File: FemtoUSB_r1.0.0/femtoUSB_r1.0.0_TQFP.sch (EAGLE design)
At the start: 24 parts, among them IC1 ATSAMD21E18A-AU

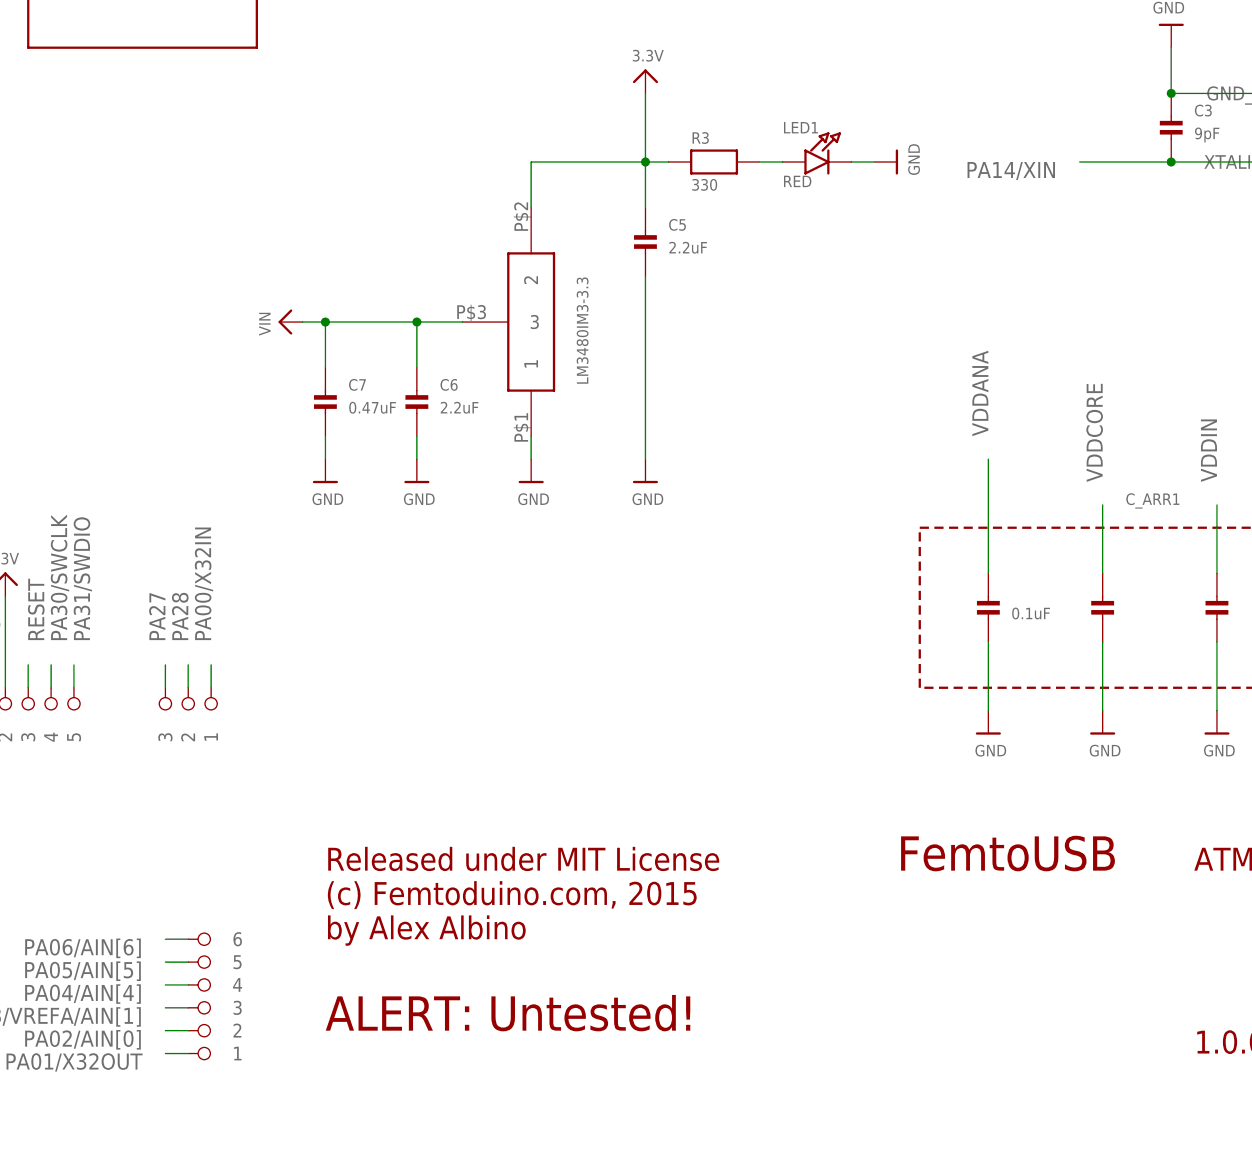
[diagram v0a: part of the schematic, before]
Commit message: Corrected the Make and model of the LDO Voltage Regulator. Board now powers on.
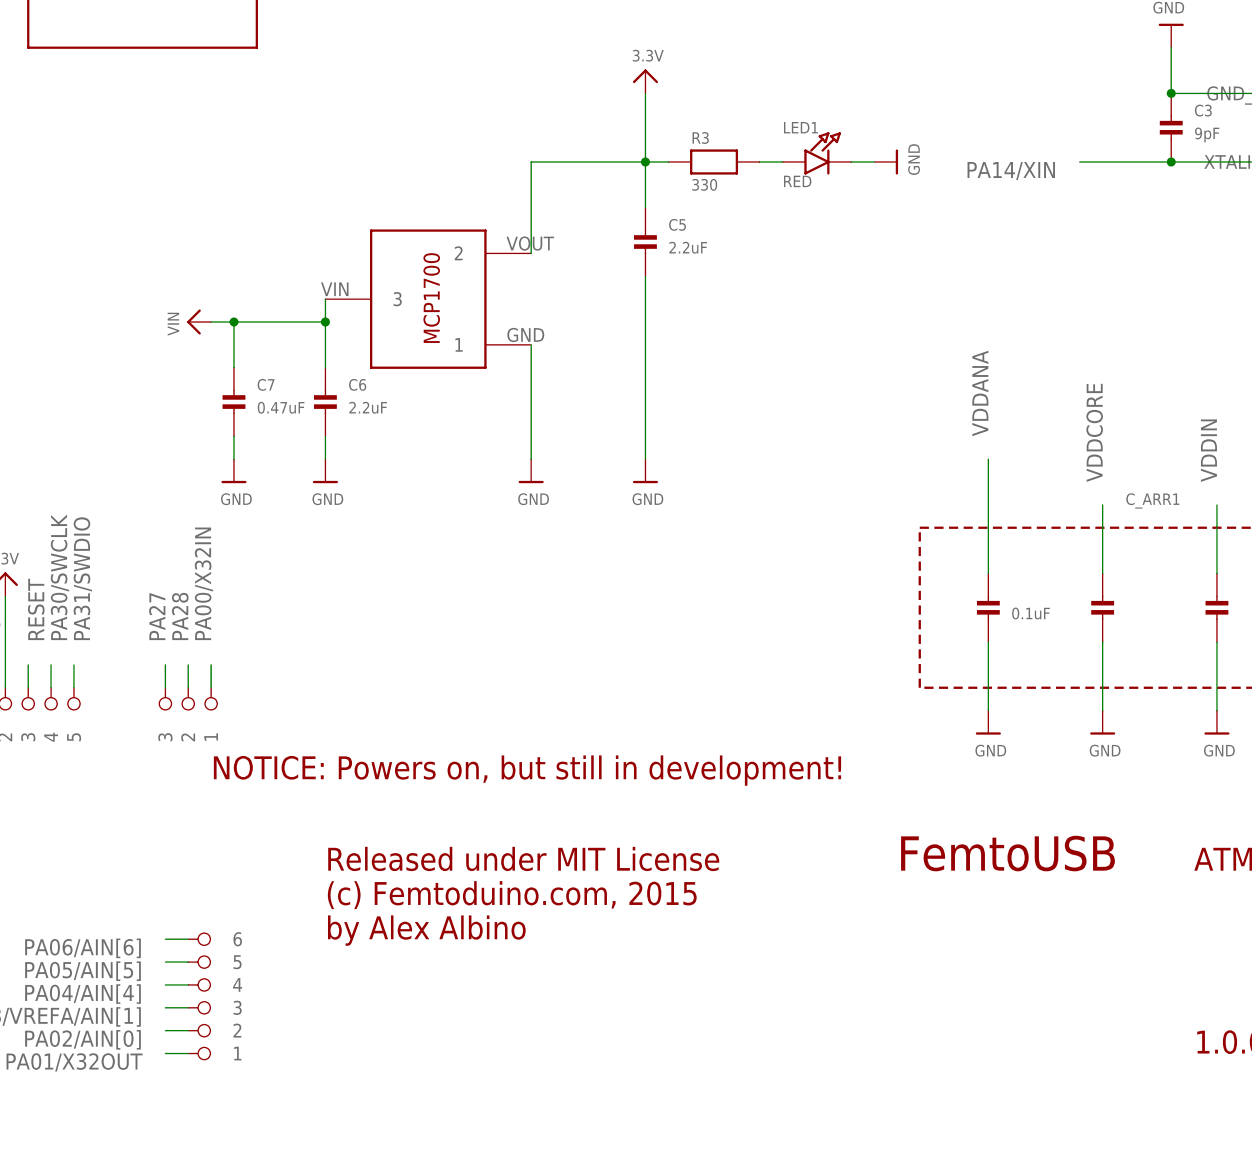
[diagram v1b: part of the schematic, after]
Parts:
- LDO_VREG: value LM3480 -> MCP1700T-3302E/TT; device ti-lm3480:LM3480 -> MCP1700T-3302E_TT:MCP1700T-3302E/TT
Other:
- note added: "NOTICE: Powers on, but still in development!"
- note removed: "ALERT: Untested!"
- moved on the sheet: C6, C7
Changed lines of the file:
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@@
 <part name="U$26" library="microbuilder" deviceset="GND" device=""/>
 <part name="U$27" library="microbuilder" deviceset="GND" device=""/>
-<part name="LDO_VREG" library="ti-lm3480" deviceset="LM3480" device=""/>
+<part name="LDO_VREG" library="MCP1700T-3302E_TT" deviceset="MCP1700T-3302E/TT" device=""/>
 <part name="U$3" library="microbuilder" deviceset="GND" device=""/>
 <part name="C5" library="microbuilder" deviceset="CAP_CERAMIC" device="_0402MP" value="2.2uF"/>
@@
 (c) Femtoduino.com, 2015
 by Alex Albino</text>
-<text x="86.36" y="10.16" size="3.81" layer="94" font="vector">ALERT: Untested!</text>
+<text x="73.66" y="38.1" size="2.54" layer="94" font="vector">NOTICE: Powers on, but still in development!</text>
 </plain>
 <instances>
@@
 <instance part="U$26" gate="G$1" x="180.34" y="121.92" rot="R180"/>
 <instance part="U$27" gate="G$1" x="226.06" y="99.06"/>
-<instance part="LDO_VREG" gate="G$1" x="106.68" y="96.52" rot="R270"/>
+<instance part="LDO_VREG" gate="G$1" x="104.14" y="99.06" rot="R180"/>
 <instance part="U$3" gate="G$1" x="149.86" y="106.68" rot="R90"/>
 <instance part="C5" gate="G$1" x="121.92" y="96.52"/>
 <instance part="U$4" gate="G$1" x="121.92" y="116.84"/>
 <instance part="U$28" gate="G$1" x="109.22" y="71.12"/>
-<instance part="U$29" gate="G$1" x="81.28" y="88.9" rot="R90"/>
+<instance part="U$29" gate="G$1" x="71.12" y="88.9" rot="R90"/>
 <instance part="U$30" gate="G$1" x="121.92" y="71.12"/>
-<instance part="C6" gate="G$1" x="96.52" y="78.74"/>
-<instance part="C7" gate="G$1" x="86.36" y="78.74"/>
-<instance part="U$31" gate="G$1" x="96.52" y="71.12"/>
-<instance part="U$32" gate="G$1" x="86.36" y="71.12"/>
+<instance part="C6" gate="G$1" x="86.36" y="78.74"/>
+<instance part="C7" gate="G$1" x="76.2" y="78.74"/>
+<instance part="U$31" gate="G$1" x="86.36" y="71.12"/>
+<instance part="U$32" gate="G$1" x="76.2" y="71.12"/>
 <instance part="U$33" gate="G$1" x="198.12" y="43.18"/>
 <instance part="U$34" gate="G$1" x="172.72" y="165.1" rot="R90"/>
@@
 <pinref part="LDO_VREG" gate="G$1" pin="1"/>
 <pinref part="U$28" gate="G$1" pin="GND"/>
-<wire x1="109.22" y1="73.66" x2="109.22" y2="76.2" width="0.1524" layer="91"/>
+<wire x1="109.22" y1="73.66" x2="109.22" y2="86.36" width="0.1524" layer="91"/>
 </segment>
 <segment>
@@
 <pinref part="C6" gate="G$1" pin="P$2"/>
 <pinref part="U$31" gate="G$1" pin="GND"/>
-<wire x1="96.52" y1="76.2" x2="96.52" y2="73.66" width="0.1524" layer="91"/>
+<wire x1="86.36" y1="76.2" x2="86.36" y2="73.66" width="0.1524" layer="91"/>
 </segment>
 <segment>
 <pinref part="C7" gate="G$1" pin="P$2"/>
 <pinref part="U$32" gate="G$1" pin="GND"/>
-<wire x1="86.36" y1="76.2" x2="86.36" y2="73.66" width="0.1524" layer="91"/>
+<wire x1="76.2" y1="76.2" x2="76.2" y2="73.66" width="0.1524" layer="91"/>
 </segment>
 <segment>
@@
 <pinref part="U$4" gate="G$1" pin="3.3V"/>
 <pinref part="LDO_VREG" gate="G$1" pin="2"/>
-<wire x1="109.22" y1="101.6" x2="109.22" y2="106.68" width="0.1524" layer="91"/>
+<wire x1="109.22" y1="96.52" x2="109.22" y2="106.68" width="0.1524" layer="91"/>
 <wire x1="109.22" y1="106.68" x2="121.92" y2="106.68" width="0.1524" layer="91"/>
 </segment>
@@
 <segment>
 <pinref part="LDO_VREG" gate="G$1" pin="3"/>
-<wire x1="101.6" y1="88.9" x2="96.52" y2="88.9" width="0.1524" layer="91"/>
-<junction x="96.52" y="88.9"/>
-<wire x1="96.52" y1="88.9" x2="86.36" y2="88.9" width="0.1524" layer="91"/>
+<wire x1="86.36" y1="91.44" x2="86.36" y2="88.9" width="0.1524" layer="91"/>
 <junction x="86.36" y="88.9"/>
-<wire x1="86.36" y1="88.9" x2="83.82" y2="88.9" width="0.1524" layer="91"/>
+<wire x1="86.36" y1="88.9" x2="76.2" y2="88.9" width="0.1524" layer="91"/>
+<junction x="76.2" y="88.9"/>
+<wire x1="76.2" y1="88.9" x2="73.66" y2="88.9" width="0.1524" layer="91"/>
 <pinref part="U$29" gate="G$1" pin="VIN"/>
+<wire x1="76.2" y1="88.9" x2="76.2" y2="83.82" width="0.1524" layer="91"/>
 <wire x1="86.36" y1="88.9" x2="86.36" y2="83.82" width="0.1524" layer="91"/>
-<wire x1="96.52" y1="88.9" x2="96.52" y2="83.82" width="0.1524" layer="91"/>
 <pinref part="C6" gate="G$1" pin="P$1"/>
 <pinref part="C7" gate="G$1" pin="P$1"/>

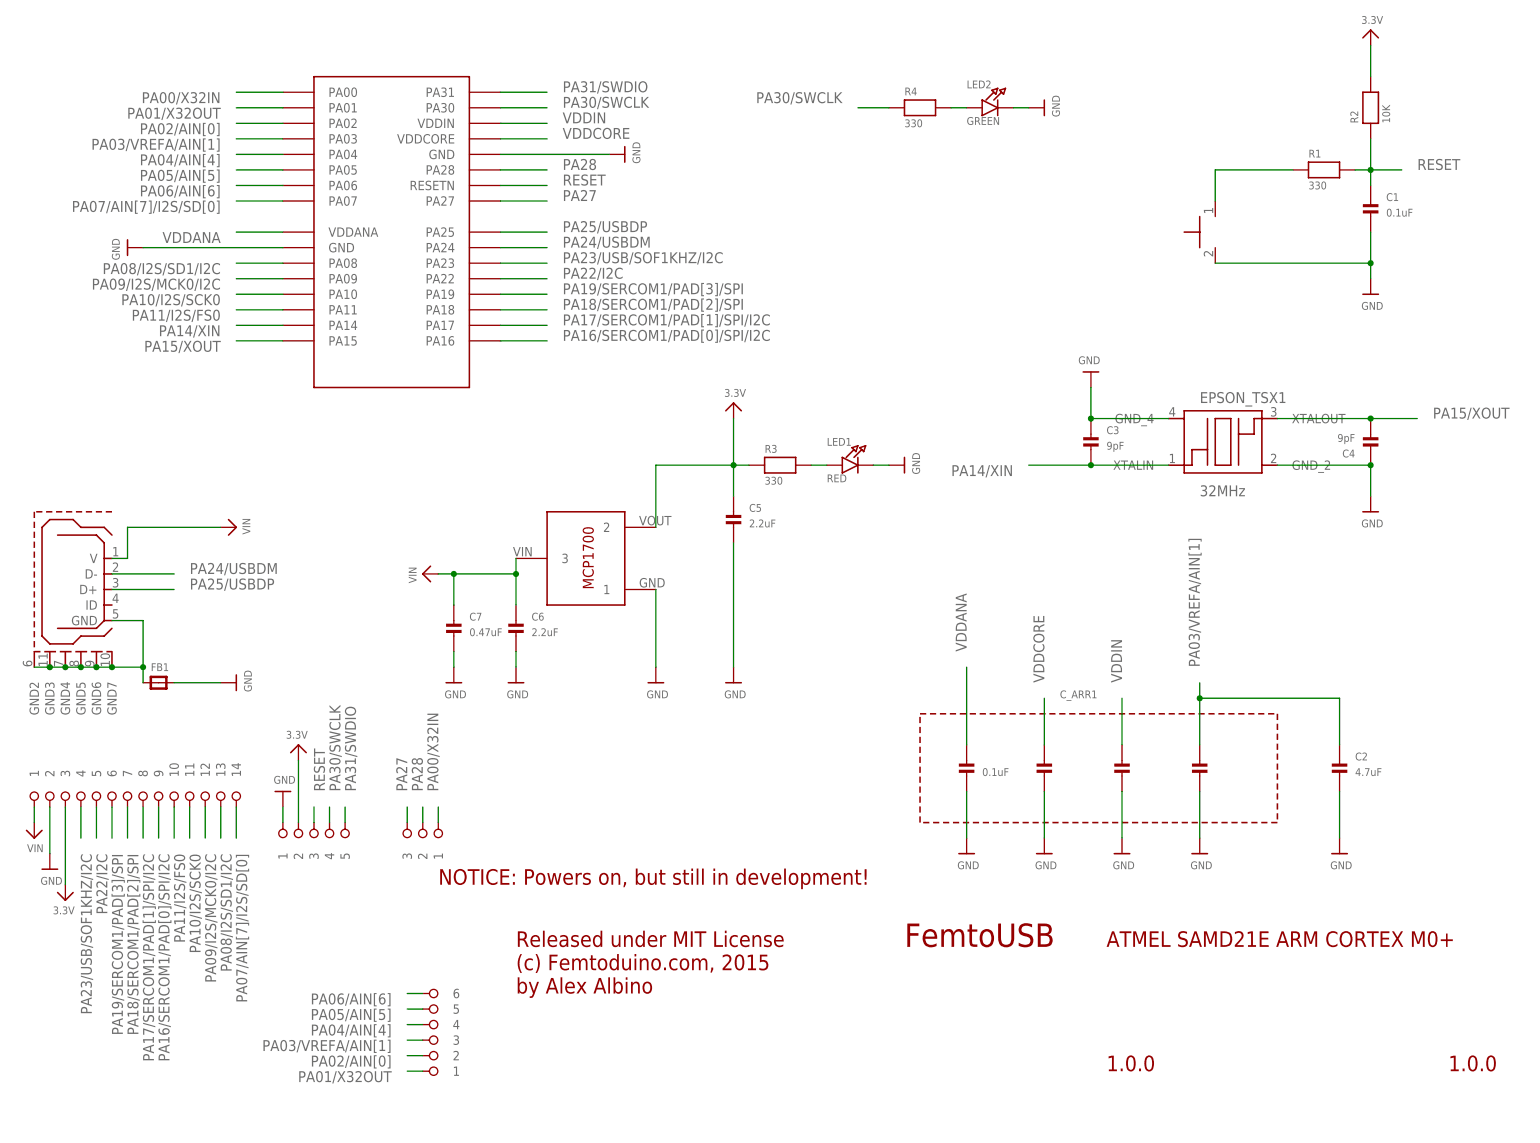
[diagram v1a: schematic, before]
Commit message: Corrected the snubbing circuits by adding the missing 10uH inductor, and two missing 10uF capacitors. Also corrected the connection from VDDIN pin to 3V3
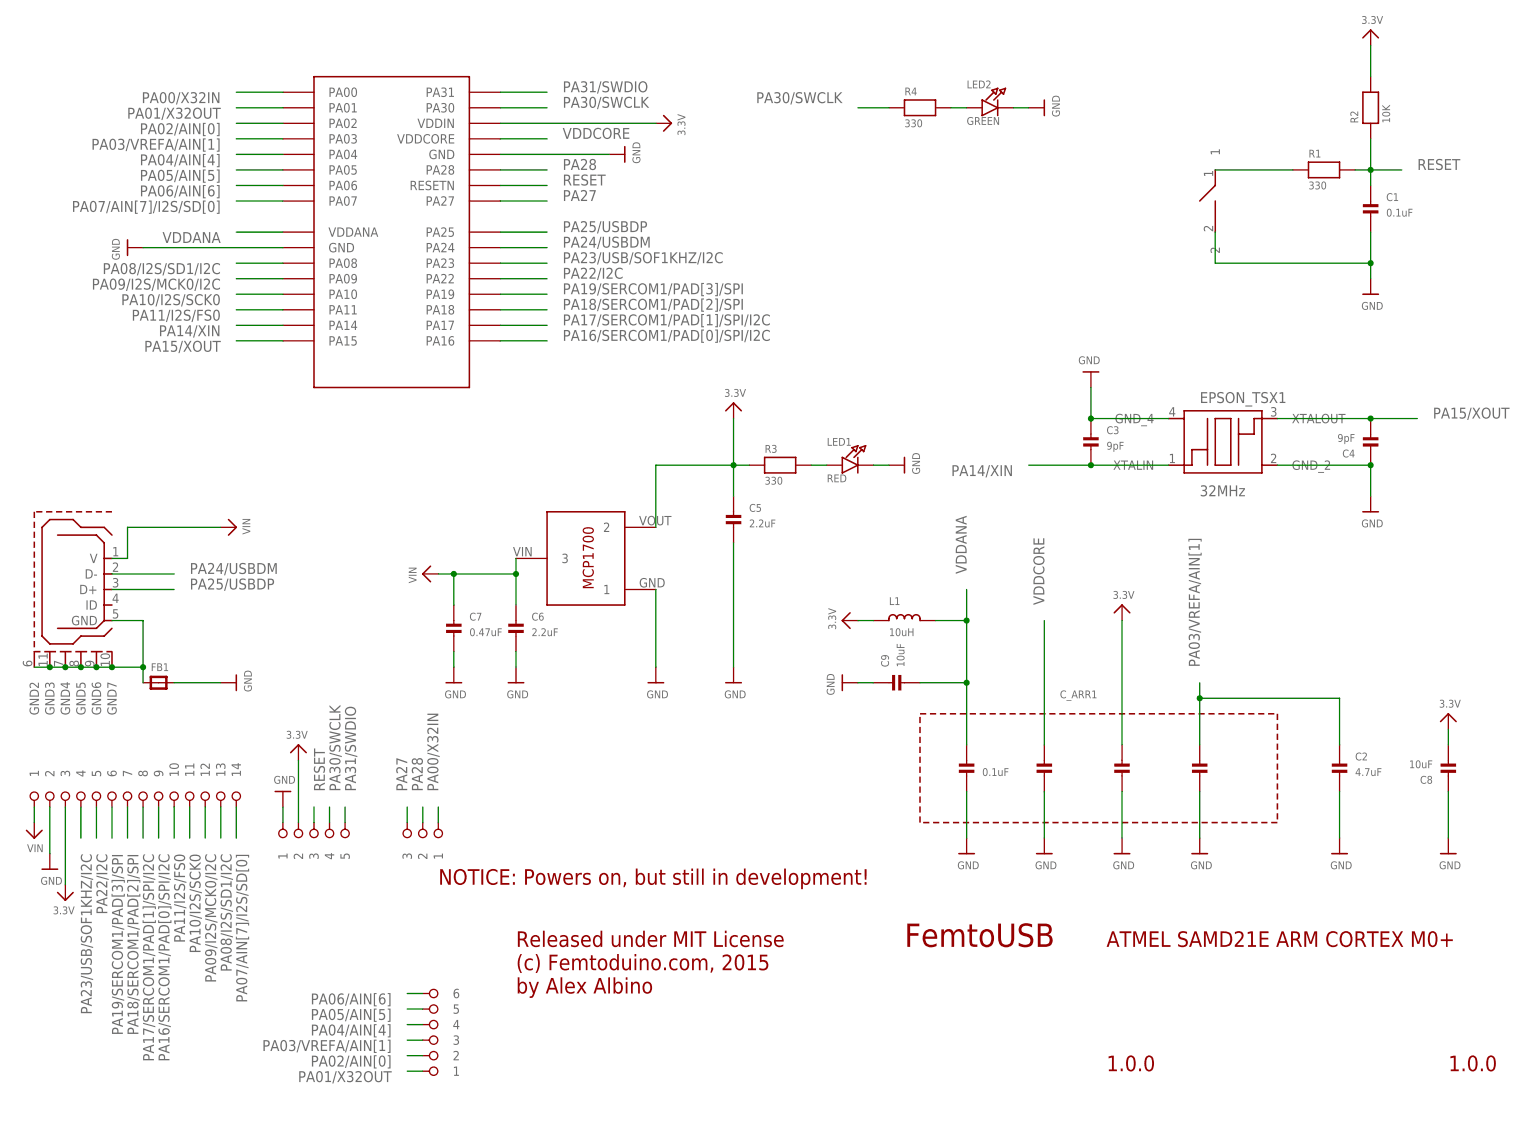
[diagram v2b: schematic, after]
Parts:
- added C8, C9: 10uF, microbuilder:CAP_CERAMIC_0402MP
- added L1: 10uH, microbuilder:INDUCTOR_0603MP
- BTN: device omron_tactile_switch:TACTILE_SWITCH_NO_GND_NO_BOSS -> femtoduino:SPST_SMD
- C1: DIGIKEY_PART (none) -> 445-4958-1-ND
- IC1: DIGIKEY_PART (none) -> ATSAMD21E18A-AU-ND
- R1: DIGIKEY_PART (none) -> 541-330JCT-ND
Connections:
- removed net VDDIN: C_ARR1.P$5, IC1.VDDIN
- net 3.3V: now also C8.P$2, C_ARR1.P$5, IC1.VDDIN, L1.1
- net GND: now also C8.P$1, C9.P$1
- net VDDANA: now also C9.P$2, L1.2
